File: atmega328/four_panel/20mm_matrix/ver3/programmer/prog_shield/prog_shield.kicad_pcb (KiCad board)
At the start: 2 copper layers, 72.4 x 53.3 mm, 3 parts, among them P1 CONN_3X2

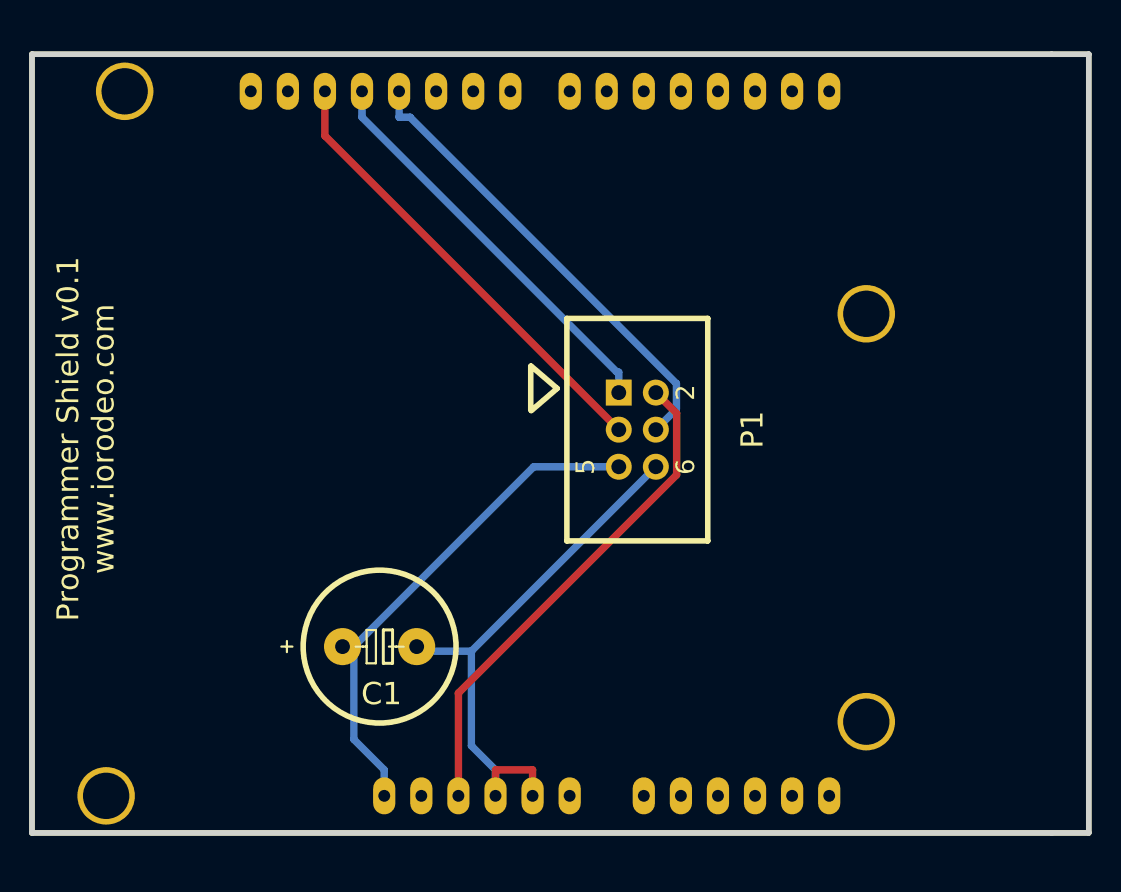
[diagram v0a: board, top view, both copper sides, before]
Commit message: move driver to panel repo
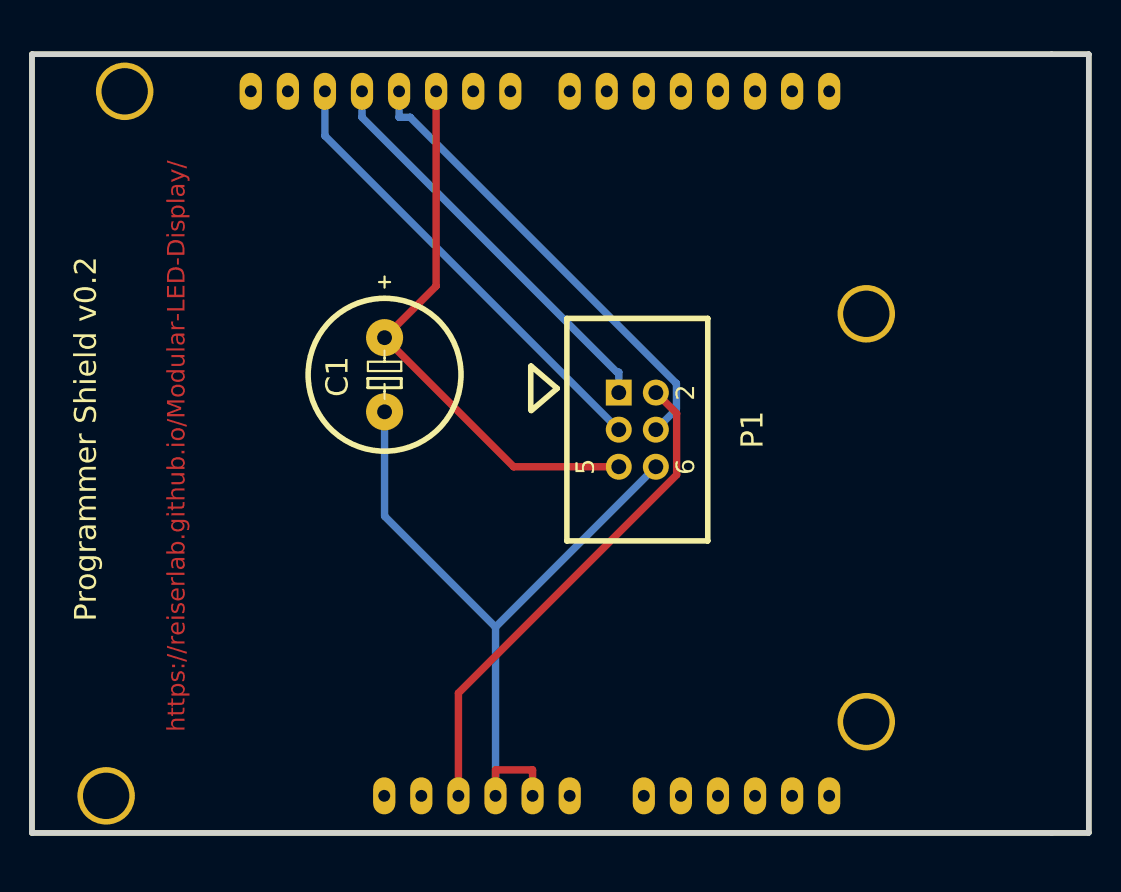
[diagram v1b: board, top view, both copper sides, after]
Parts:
- moved C1 18.6 mm to (143.8, 101.3), turned to 270 degrees
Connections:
- SHIELD1 pad 10: (no net) -> /RST
- SHIELD1 pad RST: /RST -> (no net)
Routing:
- net /GND: track 38.4 -> 51.1 mm
- net /RST: track 35.1 -> 38.0 mm
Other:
- board text added: "Programmer Shield v0.2"
- board text added: "https://reiserlab.github.io/Modular-LED-Display/"
- board text removed: "Programmer Shield v0.1 www.iorodeo.com"
